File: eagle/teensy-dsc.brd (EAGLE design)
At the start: 73.6 x 40.3 mm, 14 parts, among them J1 USB-B, J2 POWER_JACKPTH, J3 RJ45-8PTH, M1 XBEERX-VN, Q1 IRLML6344

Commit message: update date on brd to be a valid date update version on sch to match the brd
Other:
- board text added: "TeensyDSC v0.5.1 http://synfin.net/teensydsc 20150101"
- board text removed: "TeensyDSC v0.5.1 http://synfin.net/teensydsc 2014116"
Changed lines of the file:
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@@
 <?xml version="1.0" encoding="utf-8"?>
 <!DOCTYPE eagle SYSTEM "eagle.dtd">
-<eagle version="7.1.0">
+<eagle version="7.2.0">
 <drawing>
 <settings>
@@
 <text x="34.417" y="27.432" size="1.016" layer="22" rot="MR180">TeensyDSC v0.5.1
 http://synfin.net/teensydsc
-2014116</text>
+20150101</text>
 <text x="72.136" y="10.414" size="1.016" layer="26" rot="MR0">S/N:</text>
 <rectangle x1="54.61" y1="9.906" x2="68.58" y2="14.986" layer="26" rot="R180"/>

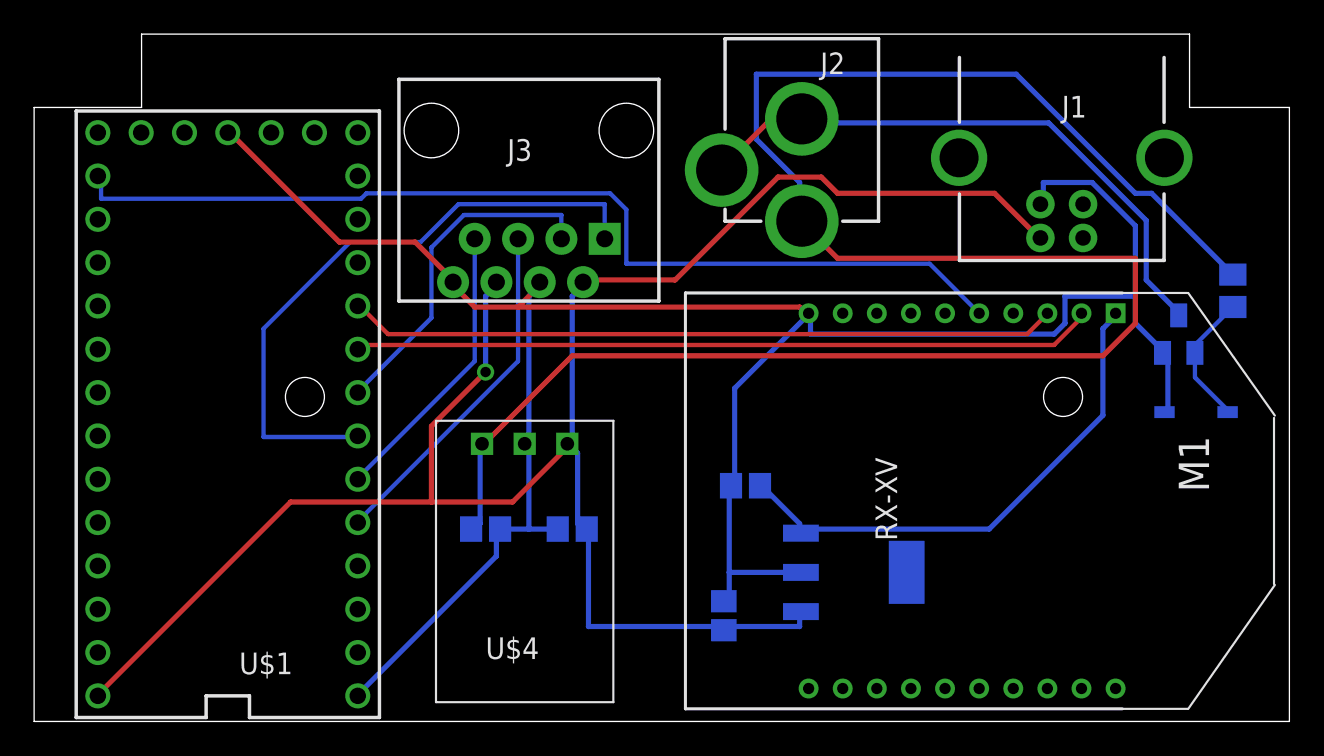
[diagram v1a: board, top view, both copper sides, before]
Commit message: trim board a little to better fit in the enclosure
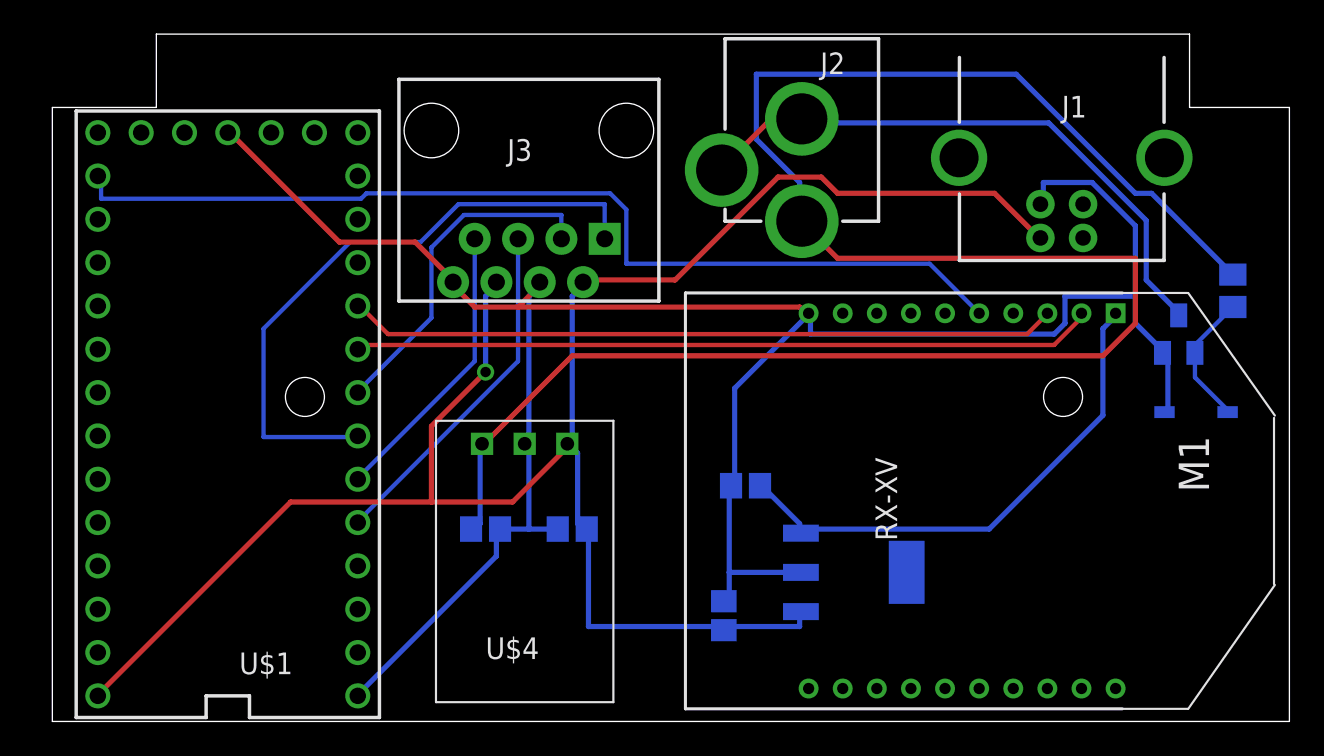
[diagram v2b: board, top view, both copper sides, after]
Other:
- board size 73.6 x 40.3 mm -> 72.5 x 40.3 mm
- board text added: "TeensyDSC v0.5.2 http://synfin.net/teensydsc 20150105"
- board text removed: "TeensyDSC v0.5.1 http://synfin.net/teensydsc 20150101"
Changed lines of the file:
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@@
 <?xml version="1.0" encoding="utf-8"?>
 <!DOCTYPE eagle SYSTEM "eagle.dtd">
-<eagle version="7.2.0">
+<eagle version="7.1.0">
 <drawing>
 <settings>
@@
 <setting verticaltext="up"/>
 </settings>
-<grid distance="0.05" unitdist="inch" unit="mil" style="lines" multiple="1" display="no" altdistance="0.01" altunitdist="inch" altunit="mil"/>
+<grid distance="0.05" unitdist="inch" unit="inch" style="lines" multiple="1" display="no" altdistance="0.01" altunitdist="inch" altunit="inch"/>
 <layers>
 <layer number="1" name="Top" color="4" fill="1" visible="yes" active="yes"/>
@@
 <board>
 <plain>
-<wire x1="0.2" y1="6.5" x2="73.8" y2="6.5" width="0" layer="20"/>
+<wire x1="1.27" y1="6.5" x2="73.8" y2="6.5" width="0" layer="20"/>
 <wire x1="73.8" y1="6.5" x2="73.8" y2="42.5" width="0" layer="20"/>
 <hole x="16.0782" y="25.527" drill="2.286"/>
 <hole x="60.5282" y="25.527" drill="2.286"/>
-<text x="34.417" y="27.432" size="1.016" layer="22" rot="MR180">TeensyDSC v0.5.1
+<text x="34.417" y="27.432" size="1.016" layer="22" rot="MR180">TeensyDSC v0.5.2
 http://synfin.net/teensydsc
-20150101</text>
+20150105</text>
 <text x="72.136" y="10.414" size="1.016" layer="26" rot="MR0">S/N:</text>
 <rectangle x1="54.61" y1="9.906" x2="68.58" y2="14.986" layer="26" rot="R180"/>
 <text x="26.67" y="10.16" size="1.27" layer="25">U$4</text>
-<wire x1="67.945" y1="46.8" x2="6.5" y2="46.8" width="0" layer="20"/>
-<wire x1="0.2" y1="42.5" x2="0.2" y2="6.5" width="0" layer="20"/>
-<wire x1="0.2" y1="42.5" x2="6.5" y2="42.5" width="0" layer="20"/>
-<wire x1="6.5" y1="42.5" x2="6.5" y2="46.8" width="0" layer="20"/>
+<wire x1="67.945" y1="46.8" x2="7.366" y2="46.8" width="0" layer="20"/>
+<wire x1="1.27" y1="42.5" x2="1.27" y2="6.5" width="0" layer="20"/>
+<wire x1="1.27" y1="42.5" x2="7.366" y2="42.5" width="0" layer="20"/>
+<wire x1="7.366" y1="42.5" x2="7.366" y2="46.8" width="0" layer="20"/>
 <wire x1="67.945" y1="46.8" x2="67.945" y2="42.5" width="0" layer="20"/>
 <wire x1="67.945" y1="42.5" x2="73.8" y2="42.5" width="0" layer="20"/>
